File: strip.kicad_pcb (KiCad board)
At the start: 4 copper layers, 66 x 18 mm, 44 parts, among them J102 WAGO-2065, J103 WAGO-2065, J104 WAGO-2065, J105 CORTEX-DEBUG, J106 JAE DX07S016JA1R1500, SW101 SW_Push, SW102 SW_Push, U101 74AHC1G125, U102 ATSAMD51G, U103 AP2112K-3.3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

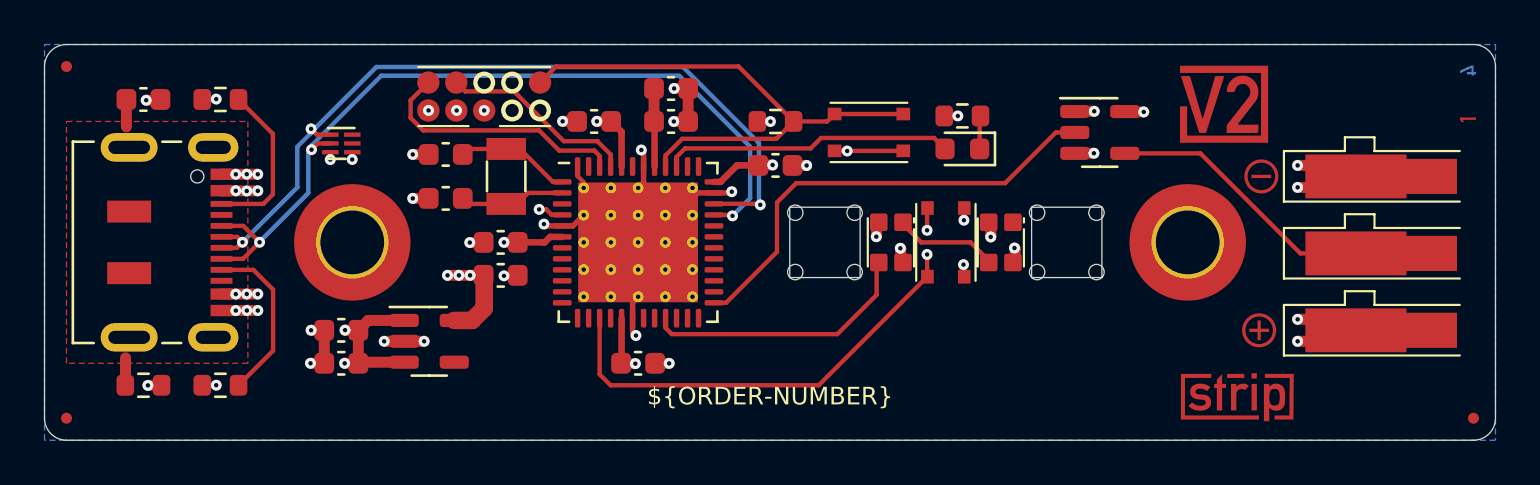
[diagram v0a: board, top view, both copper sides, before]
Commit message: Update to KiCad 7.0
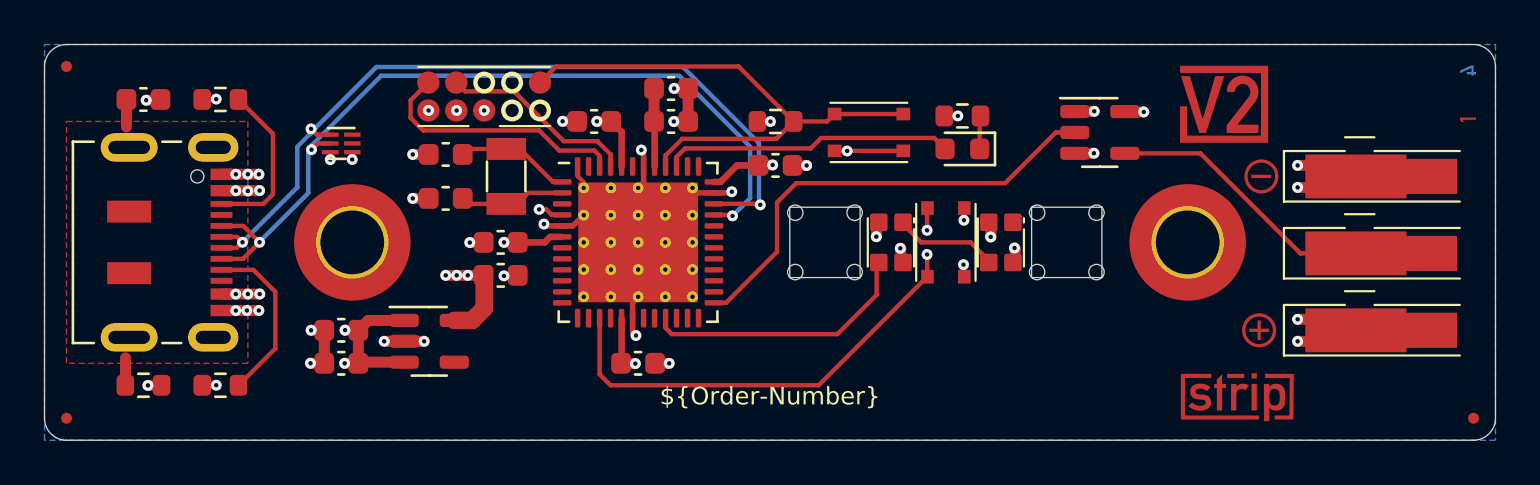
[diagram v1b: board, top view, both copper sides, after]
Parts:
- J106: value JAE DX07S016JA1R1500 -> JAE_DX07S016JA3; footprint V2_Connector_USB:JAE_DX07S016JA1R1500 -> V2_Connector_USB:JAE_DX07S016JA3
- SPACER101, SPACER102: value 977?2434030 -> 3mm
